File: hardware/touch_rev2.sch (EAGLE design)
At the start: 17 parts, among them SW1 SWITCH, SW2 SWITCH, U1 MPR121-TOUCH-CONTROLLER, U2 M41T82ZM6F, U3 CAPACITIVE-WHEEL-8, X1 32.768kHz

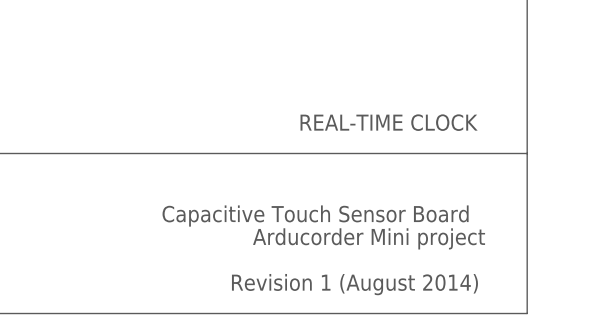
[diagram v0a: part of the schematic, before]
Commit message: Added motherboard rev1 and capacitive touch board rev2
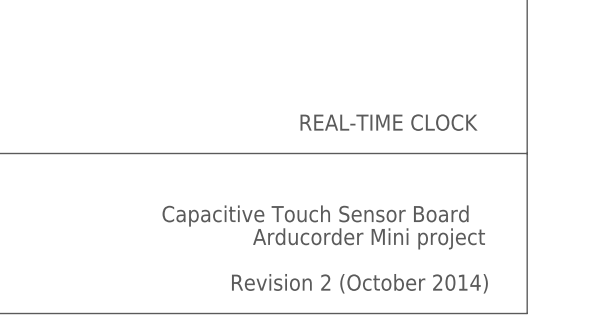
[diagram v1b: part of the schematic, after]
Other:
- note added: "Revision 2 (October 2014)"
- note removed: "Revision 1 (August 2014)"
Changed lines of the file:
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@@
 <setting verticaltext="up"/>
 </settings>
-<grid distance="0.1" unitdist="inch" unit="inch" style="lines" multiple="1" display="yes" altdistance="0.01" altunitdist="inch" altunit="inch"/>
+<grid distance="0.1" unitdist="inch" unit="inch" style="lines" multiple="1" display="no" altdistance="0.01" altunitdist="inch" altunit="inch"/>
 <layers>
 <layer number="1" name="Top" color="4" fill="1" visible="no" active="no"/>
@@
 <text x="-101.6" y="-93.98" size="1.778" layer="97">Designed by: Peter Jansen</text>
 <text x="-101.6" y="-96.52" size="1.778" layer="97">http://www.tricorderproject.org </text>
-<text x="68.58" y="-96.52" size="1.778" layer="97">Revision 1 (August 2014)</text>
+<text x="68.58" y="-96.52" size="1.778" layer="97">Revision 2 (October 2014)</text>
 <text x="71.12" y="-91.44" size="1.778" layer="97">Arducorder Mini project</text>
 <text x="60.96" y="-88.9" size="1.778" layer="97">Capacitive Touch Sensor Board</text>
